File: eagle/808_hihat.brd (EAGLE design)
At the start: 100 x 80 mm, 127 parts, among them IC1 TL072P, IC2 TL072P, U4 4584N

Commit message: baby steps
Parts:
- moved C2*1 22.2 mm to (34.3, 20.3), turned to 270 degrees
- moved R142* 14.0 mm to (69.8, 68.6), turned to 0 degrees
- moved C1*1 12.7 mm to (34.3, 26.7), turned to 180 degrees
- moved R40*1 12.7 mm to (29.2, 24.1), turned to 180 degrees
- moved R161* 11.7 mm to (87.6, 17.8)
- moved R144* 11.5 mm to (68.6, 59.7), turned to 0 degrees
- moved C5*1 9.25 mm to (7.62, 21.6), turned to 0 degrees
- moved D14* 8.98 mm to (66.0, 24.1)
- moved C6*1 8.52 mm to (14.0, 8.89), turned to 90 degrees
- moved R55*1 8.03 mm to (44.5, 24.1), turned to 0 degrees
- moved C70* 7.18 mm to (72.4, 26.7)
- moved R136* 6.84 mm to (53.3, 57.1), turned to 270 degrees
- moved R48*1 6.48 mm to (26.7, 36.8)
- moved C3*1 6.35 mm to (19.1, 8.89), turned to 270 degrees
- moved C1 6.35 mm to (40.6, 31.8)
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
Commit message: closer
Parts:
- moved R156* 18.2 mm to (83.8, 39.4)
- moved R13* 16.7 mm to (11.4, 57.1)
- moved R160* 5.68 mm to (91.4, 52.1)
- moved C80* 4.58 mm to (90.2, 47.0)
- moved R158* 4.58 mm to (73.7, 35.6)
- moved D2 3.81 mm to (7.62, 64.8)
- moved C3 2.84 mm to (77.5, 33.0)
- moved CH_TRIG 2.84 mm to (6.35, 71.1)
- moved R154* 2.84 mm to (91.4, 12.7)
- moved R16* 2.84 mm to (10.2, 64.8)
- moved Q4* 2.54 mm to (14.0, 44.5)
- moved R11* 2.54 mm to (14.0, 52.1)
- moved CH_OUT 2.54 mm to (85.1, 10.2)
- moved IC1 2.54 mm to (85.1, 31.8)
- moved Q31* 1.80 mm to (92.7, 24.1)
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
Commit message: three routes left
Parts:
- R153*: device TR808clone:0207/2V -> rcl:0207/5V
- moved C83* 21.3 mm to (93.5, 33.0), turned to 270 degrees
- moved R48*1 20.3 mm to (8.13, 28.4), turned to 180 degrees
- moved R50*1 14.8 mm to (3.05, 28.4), turned to 270 degrees
- moved C6*1 10.1 mm to (6.86, 16.0), turned to 0 degrees
- moved C2 9.25 mm to (96.5, 24.1), turned to 90 degrees
- moved R132* 8.98 mm to (35.6, 66.0)
- moved R141* 8.52 mm to (53.3, 69.8)
- moved R46*1 8.03 mm to (16.5, 38.1)
- moved R40*1 7.73 mm to (26.7, 31.8), turned to 270 degrees
- moved R140* 7.27 mm to (58.9, 47.2)
- moved R136* 6.86 mm to (53.6, 64.0), turned to 90 degrees
- moved R35*1 6.48 mm to (29.2, 38.1), turned to 0 degrees
- moved C80* 6.35 mm to (90.2, 53.3)
- moved R173* 6.25 mm to (57.9, 50.5), turned to 180 degrees
- moved R44*1 5.92 mm to (7.11, 19.1), turned to 0 degrees
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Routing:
- net GND: track 0.00 -> 511.3 mm
- net +12V: track 0.00 -> 308.0 mm, vias 0 -> 2
- net -12V: track 0.00 -> 108.6 mm
- net N$2: track 0.00 -> 86.8 mm
- net N$603: track 0.00 -> 82.5 mm
- net N$600: track 0.00 -> 78.2 mm
- net N$592: track 0.00 -> 64.7 mm
- net N$375: track 0.00 -> 58.7 mm
- net +5V: track 0.00 -> 51.7 mm
- net N$563: track 0.00 -> 50.9 mm
- net N$209: track 0.00 -> 45.4 mm
- net TO_HH: track 0.00 -> 42.3 mm, vias 0 -> 2
- net N$598: track 0.00 -> 42.0 mm
- net N$608: track 0.00 -> 40.2 mm
- net N$573: track 0.00 -> 34.5 mm
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
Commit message: routed but rough
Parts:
- moved R142* 2.41 mm to (67.6, 69.3), turned to 180 degrees
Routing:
- net N$220: track 7.34 -> 73.2 mm, vias 0 -> 2
- net GND: track 511.3 -> 552.7 mm, vias 0 -> 4
- net N$581: track 25.7 -> 26.5 mm
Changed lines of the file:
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@@
 <element name="R140*" library="TR808clone" package="0207/5V" value="33K" x="58.928" y="47.244"/>
 <element name="R141*" library="TR808clone" package="0207/5V" value="33K" x="53.34" y="69.85"/>
-<element name="R142*" library="TR808clone" package="0207/5V" value="33K" x="69.85" y="68.58"/>
+<element name="R142*" library="TR808clone" package="0207/5V" value="33K" x="67.564" y="69.342" rot="R180"/>
 <element name="R143*" library="TR808clone" package="0207/5V" value="33K" x="47.752" y="41.148" rot="R180"/>
 <element name="R144*" library="TR808clone" package="0207/5V" value="33K" x="68.58" y="59.69"/>
@@
 <contactref element="R142*" pad="1"/>
 <wire x1="69.85" y1="66.04" x2="68.58" y2="67.31" width="0.635" layer="16"/>
-<wire x1="68.58" y1="67.31" x2="67.31" y2="68.58" width="0.635" layer="16"/>
+<wire x1="68.58" y1="67.31" x2="70.104" y2="69.342" width="0.635" layer="16"/>
 <wire x1="64.008" y1="64.516" x2="63.246" y2="54.864" width="0.635" layer="16"/>
 <wire x1="63.246" y1="54.864" x2="63.246" y2="50.546" width="0.635" layer="16"/>
@@
 <wire x1="3.588" y1="22.86" x2="1.04775" y2="22.86" width="0.8128" layer="16"/>
 <wire x1="1.04775" y1="22.86" x2="0.79375" y2="22.606" width="0.8128" layer="16"/>
-<wire x1="74.93" y1="41.91" x2="69.215" y2="56.515" width="0" layer="19" extent="16-16"/>
-<wire x1="22.86" y1="34.29" x2="22.86" y2="41.91" width="0" layer="19" extent="1-1"/>
-<wire x1="17.78" y1="52.07" x2="25.4" y2="49.53" width="0" layer="19" extent="1-1"/>
+<wire x1="22.86" y1="41.91" x2="13.97" y2="41.91" width="0.8128" layer="16"/>
+<wire x1="22.86" y1="41.91" x2="22.86" y2="39.878" width="0.8128" layer="16"/>
+<wire x1="22.86" y1="39.878" x2="23.114" y2="39.624" width="0.8128" layer="16"/>
+<via x="23.114" y="39.624" extent="1-16" drill="0.6" shape="square"/>
+<wire x1="23.114" y1="39.624" x2="23.114" y2="36.576" width="0.8128" layer="1"/>
+<via x="23.114" y="36.576" extent="1-16" drill="0.6" shape="square"/>
+<wire x1="23.114" y1="36.576" x2="23.114" y2="34.544" width="0.8128" layer="16"/>
+<wire x1="23.114" y1="34.544" x2="22.86" y2="34.29" width="0.8128" layer="16"/>
+<wire x1="74.93" y1="41.91" x2="76.962" y2="41.91" width="0.8128" layer="16"/>
+<wire x1="76.962" y1="41.91" x2="77.47" y2="41.402" width="0.8128" layer="16"/>
+<via x="77.47" y="41.402" extent="1-16" drill="0.6" shape="square"/>
+<wire x1="77.47" y1="41.402" x2="77.47" y2="46.736" width="0.8128" layer="1"/>
+<wire x1="77.47" y1="46.736" x2="80.01" y2="49.276" width="0.8128" layer="1"/>
+<wire x1="80.01" y1="49.276" x2="80.01" y2="58.166" width="0.8128" layer="1"/>
+<wire x1="80.01" y1="58.166" x2="80.518" y2="58.674" width="0.8128" layer="1"/>
+<via x="80.518" y="58.674" extent="1-16" drill="0.6" shape="square"/>
+<wire x1="80.518" y1="58.674" x2="80.744" y2="58.674" width="0.8128" layer="16"/>
+<wire x1="80.744" y1="58.674" x2="83.03" y2="60.96" width="0.8128" layer="16"/>
 </signal>
 <signal name="N$219">
@@
 <wire x1="67.31" y1="21.59" x2="69.37" y2="21.59" width="0.635" layer="16"/>
 <wire x1="66.04" y1="20.32" x2="67.31" y2="21.59" width="0.635" layer="16"/>
-<wire x1="69.37" y1="21.59" x2="72.39" y2="68.58" width="0" layer="19" extent="1-1"/>
+<wire x1="65.024" y1="69.342" x2="62.738" y2="69.342" width="0.8128" layer="16"/>
+<via x="62.738" y="69.342" extent="1-16" drill="0.6" shape="square"/>
+<wire x1="62.738" y1="69.342" x2="62.738" y2="69.088" width="0.8128" layer="1"/>
+<wire x1="62.738" y1="69.088" x2="66.294" y2="65.532" width="0.8128" layer="1"/>
+<wire x1="66.294" y1="65.532" x2="66.294" y2="63.246" width="0.8128" layer="1"/>
+<wire x1="66.294" y1="63.246" x2="64.262" y2="61.214" width="0.8128" layer="1"/>
+<wire x1="64.262" y1="61.214" x2="64.262" y2="60.96" width="0.8128" layer="1"/>
+<wire x1="64.262" y1="60.96" x2="62.992" y2="59.69" width="0.8128" layer="1"/>
+<wire x1="62.992" y1="59.69" x2="62.992" y2="45.974" width="0.8128" layer="1"/>
+<wire x1="62.992" y1="45.974" x2="65.024" y2="43.942" width="0.8128" layer="1"/>
+<wire x1="65.024" y1="43.942" x2="68.58" y2="43.942" width="0.8128" layer="1"/>
+<wire x1="68.58" y1="43.942" x2="70.358" y2="42.164" width="0.8128" layer="1"/>
+<wire x1="70.358" y1="42.164" x2="70.358" y2="27.432" width="0.8128" layer="1"/>
+<wire x1="70.358" y1="27.432" x2="66.802" y2="23.876" width="0.8128" layer="1"/>
+<wire x1="66.802" y1="23.876" x2="65.786" y2="23.876" width="0.8128" layer="1"/>
+<wire x1="65.786" y1="23.876" x2="62.23" y2="20.32" width="0.8128" layer="1"/>
+<via x="62.23" y="20.32" extent="1-16" drill="0.6" shape="square"/>
+<wire x1="62.23" y1="20.32" x2="62.23" y2="19.53" width="0.8128" layer="16"/>
+<wire x1="62.23" y1="19.53" x2="63.5" y2="18.26" width="0.8128" layer="16"/>
 </signal>
 <signal name="OH_OUT">
@@
 <wire x1="10.414" y1="21.336" x2="10.16" y2="19.812" width="0.8128" layer="16"/>
 <wire x1="10.16" y1="19.812" x2="9.652" y2="19.05" width="0.8128" layer="16"/>
-<wire x1="3.048" y1="25.908" x2="5.588" y2="22.606" width="0.8128" layer="16"/>
-<wire x1="5.588" y1="22.606" x2="9.652" y2="19.05" width="0.8128" layer="16"/>
+<wire x1="3.048" y1="25.908" x2="5.588" y2="22.86" width="0.8128" layer="16"/>
+<wire x1="5.588" y1="22.86" x2="9.652" y2="19.05" width="0.8128" layer="16"/>
 </signal>
 <signal name="N$15">

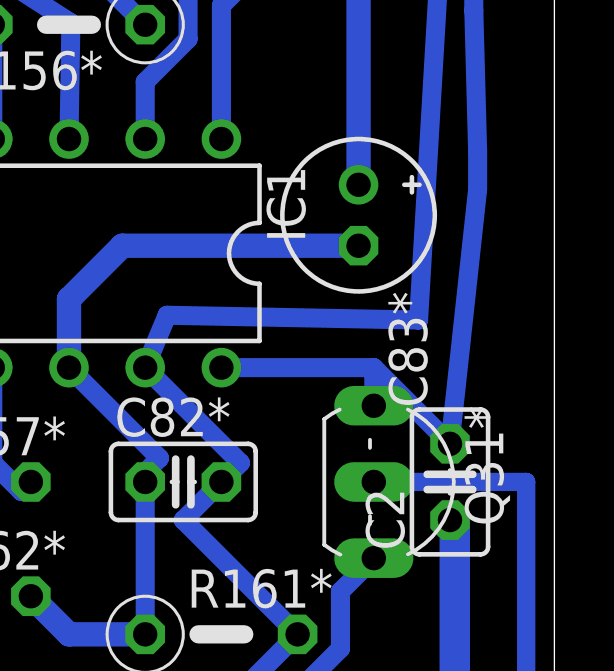
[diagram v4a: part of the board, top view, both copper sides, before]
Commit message: labeled the transistor values
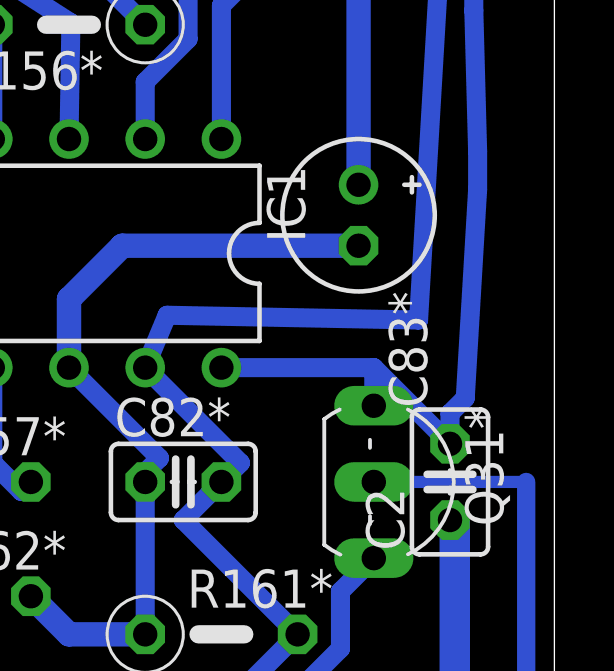
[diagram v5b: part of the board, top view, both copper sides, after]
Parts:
- Q21*, Q22*, Q23*, Q24*, Q26*, Q27*, Q28*, Q29*, Q3*, Q30*, Q31*, Q4*: value (none) -> BC546
- Q7*, Q8*: value (none) -> BC556
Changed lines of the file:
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@@
 <element name="OH_OUT" library="solpad" package="LSP11" value="LSP11" x="89.916" y="69.85"/>
 <element name="OH_TRIG" library="solpad" package="LSP11" value="LSP11" x="21.59" y="68.58"/>
-<element name="Q21*" library="transistor" package="TO92-CBE" value="" x="33.02" y="44.45" rot="R270"/>
-<element name="Q22*" library="transistor" package="TO92-CBE" value="" x="41.91" y="52.07" rot="R90"/>
-<element name="Q23*" library="transistor" package="TO92-CBE" value="" x="46.99" y="51.308" rot="R90"/>
-<element name="Q24*" library="transistor" package="TO92-CBE" value="" x="48.006" y="59.69" rot="R90"/>
-<element name="Q26*" library="transistor" package="TO92-CBE" value="" x="82.55" y="44.45"/>
-<element name="Q27*" library="transistor" package="TO92-CBE" value="" x="72.39" y="52.07" rot="R180"/>
-<element name="Q28*" library="transistor" package="TO92-CBE" value="" x="61.468" y="64.516"/>
-<element name="Q29*" library="transistor" package="TO92-CBE" value="" x="59.944" y="43.434" rot="R180"/>
-<element name="Q3*" library="transistor" package="TO92-CBE" value="" x="25.4" y="52.07" rot="R270"/>
-<element name="Q30*" library="transistor" package="TO92-CBE" value="" x="68.326" y="32.766" rot="R90"/>
-<element name="Q31*" library="transistor" package="TO92-CBE" value="" x="93.98" y="24.13" rot="R270"/>
-<element name="Q4*" library="transistor" package="TO92-CBE" value="" x="13.97" y="44.45" rot="R270"/>
-<element name="Q7*" library="transistor" package="TO92-EBC" value="" x="31.75" y="62.23" rot="R270"/>
-<element name="Q8*" library="transistor" package="TO92-EBC" value="" x="16.51" y="63.5" rot="R270"/>
+<element name="Q21*" library="transistor" package="TO92-CBE" value="BC546" x="33.02" y="44.45" rot="R270"/>
+<element name="Q22*" library="transistor" package="TO92-CBE" value="BC546" x="41.91" y="52.07" rot="R90"/>
+<element name="Q23*" library="transistor" package="TO92-CBE" value="BC546" x="46.99" y="51.308" rot="R90"/>
+<element name="Q24*" library="transistor" package="TO92-CBE" value="BC546" x="48.006" y="59.69" rot="R90"/>
+<element name="Q26*" library="transistor" package="TO92-CBE" value="BC546" x="82.55" y="44.45"/>
+<element name="Q27*" library="transistor" package="TO92-CBE" value="BC546" x="72.39" y="52.07" rot="R180"/>
+<element name="Q28*" library="transistor" package="TO92-CBE" value="BC546" x="61.468" y="64.516"/>
+<element name="Q29*" library="transistor" package="TO92-CBE" value="BC546" x="59.944" y="43.434" rot="R180"/>
+<element name="Q3*" library="transistor" package="TO92-CBE" value="BC546" x="25.4" y="52.07" rot="R270"/>
+<element name="Q30*" library="transistor" package="TO92-CBE" value="BC546" x="68.326" y="32.766" rot="R90"/>
+<element name="Q31*" library="transistor" package="TO92-CBE" value="BC546" x="93.98" y="24.13" rot="R270"/>
+<element name="Q4*" library="transistor" package="TO92-CBE" value="BC546" x="13.97" y="44.45" rot="R270"/>
+<element name="Q7*" library="transistor" package="TO92-EBC" value="BC556" x="31.75" y="62.23" rot="R270"/>
+<element name="Q8*" library="transistor" package="TO92-EBC" value="BC556" x="16.51" y="63.5" rot="R270"/>
 <element name="R1" library="TR808clone" package="0207/5V" value="22K" x="17.78" y="54.61" rot="R90"/>
 <element name="R1*" library="TR808clone" package="0207/5V" value="22K" x="19.05" y="46.99" rot="R90"/>
@@
 <wire x1="96.774" y1="3.556" x2="99.06" y2="7.62" width="0.6096" layer="16"/>
 <wire x1="99.06" y1="7.62" x2="99.06" y2="24.13" width="0.6096" layer="16"/>
-<wire x1="99.06" y1="24.13" x2="93.98" y2="24.13" width="0.6096" layer="16"/>
+<wire x1="99.06" y1="24.13" x2="93.98" y2="24.13" width="0.4064" layer="16"/>
 </signal>
 <signal name="N$595">
@@
 <wire x1="24.13" y1="77.47" x2="26.035" y2="79.375" width="0.635" layer="16"/>
 <wire x1="24.13" y1="77.47" x2="24.05" y2="77.47" width="0.635" layer="16"/>
-<wire x1="97.44075" y1="33.87725" x2="96.52" y2="25.4" width="0.635" layer="16"/>
+<wire x1="97.44075" y1="33.87725" x2="97.028" y2="26.924" width="0.635" layer="16"/>
+<wire x1="97.028" y1="26.924" x2="96.52" y2="26.416" width="0.635" layer="16"/>
+<wire x1="96.52" y1="26.416" x2="96.52" y2="25.4" width="0.635" layer="16"/>
 <wire x1="97.44075" y1="35.14725" x2="97.44075" y2="33.87725" width="0.635" layer="16"/>
 <wire x1="97.31375" y1="39.84625" x2="97.44075" y2="35.14725" width="0.635" layer="16"/>

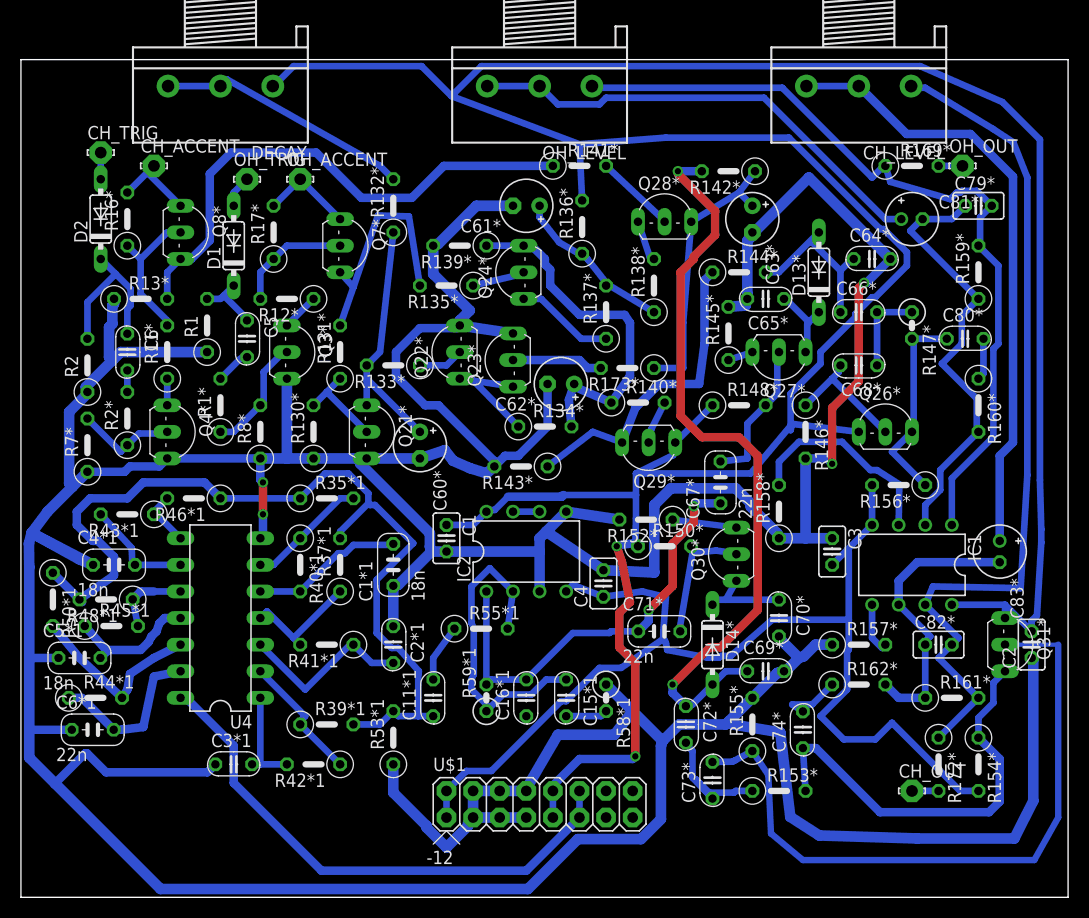
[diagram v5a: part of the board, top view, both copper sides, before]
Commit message: ready for a test run on the cnc
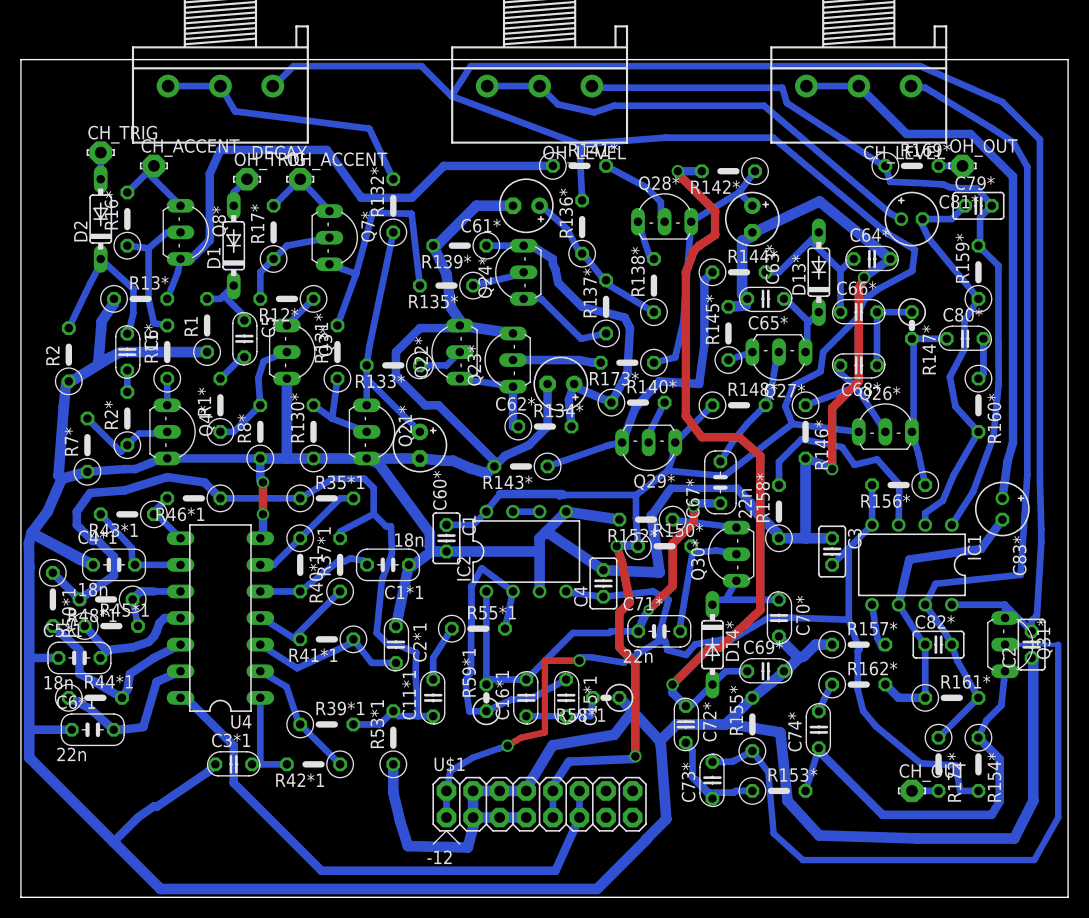
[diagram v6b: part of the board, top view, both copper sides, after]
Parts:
- moved C83* 4.07 mm to (93.7, 37.1)
- moved R2 2.05 mm to (4.57, 51.8)
- moved C74* 1.52 mm to (76.2, 16.0)
- moved Q7* 1.27 mm to (30.7, 63.0)
- moved C1*1 0.51 mm to (35.1, 31.8), turned to 180 degrees
- moved R173* 0.51 mm to (57.9, 51.1)
- moved R41*1 0.51 mm to (29.2, 24.6)
- moved R137* 0.51 mm to (55.9, 56.4)
- moved C5 0.25 mm to (21.3, 53.3)
- moved R131* 0.25 mm to (30.2, 52.1)
- moved C2*1 0.25 mm to (35.8, 24.1)
- moved R55*1 0.25 mm to (43.7, 25.7)
- turned R58*1 to 180 degrees
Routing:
- net GND: track 552.7 -> 546.2 mm
- net N$375: track 58.7 -> 54.2 mm
- net N$5: track 4.01 -> 7.89 mm
- net N$603: track 82.5 -> 79.1 mm
- net N$6: track 14.6 -> 11.5 mm
- net N$574: track 12.6 -> 9.45 mm
- net +12V: track 308.1 -> 305.1 mm
- net N$595: track 5.81 -> 2.87 mm
- net N$598: track 42.0 -> 39.1 mm
- net N$600: track 78.2 -> 75.9 mm
- net N$607: track 19.5 -> 17.6 mm
- net N$569: track 22.7 -> 24.6 mm
- net N$2: track 86.8 -> 84.9 mm
- net N$586: track 14.0 -> 12.2 mm
- net N$7: track 17.1 -> 15.5 mm
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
